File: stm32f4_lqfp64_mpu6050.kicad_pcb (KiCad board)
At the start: 2 copper layers, 35.5 x 35.2 mm, 74 parts, among them M1 ALIS-CUSTOM-PARTS_POWERPADS, M2 ALIS-CUSTOM-PARTS_POWERPADS, M3 ALIS-CUSTOM-PARTS_POWERPADS, M4 ALIS-CUSTOM-PARTS_POWERPADS, M5 ALIS-CUSTOM-PARTS_POWERPADS, Q1 CRYSTAL_50X32, Q2 BSS138, Q3 BSS138, Q4 BSS138, Q5 BSS138, Q6 BSS138, U1 STM32_STM32F10XRXT6, U2 MPU6050, U3 LP2985LV, U4 ublox_neo7, X1 CON-JST_SM04B-SRSS-TB, X2 CON-JST_SM04B-SRSS-TB, X3 CON-JST_SM04B-SRSS-TB, X4 CON-JST_SM04B-SRSS-TB, X5 CON-JST_SM04B-SRSS-TB, X6 CON-JST_SM04B-SRSS-TB, X7 CON-JST_SM04B-SRSS-TB, X8 CON-JST_SM04B-SRSS-TB

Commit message: added lots of stuff
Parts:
- added C24: 100n, Capacitors_SMD:C_0402, F.Cu at (158.5, 107.1)
- added C25: 220n, Capacitors_SMD:C_0402, F.Cu at (156.5, 113.5)
- added C26: 4u7, Capacitors_SMD:C_0805, F.Cu at (159.0, 113.5)
- added C27: 100n, Capacitors_SMD:C_0402, F.Cu at (151.8, 95.0)
- added C28: 100n, Capacitors_SMD:C_0402, F.Cu at (157.0, 93.7)
- added C29: 4.7u, Capacitors_SMD:C_0603, F.Cu at (155.7, 110.5)
- added C30: CP, alis_parts:DSK-3R3H204T614-H2L, B.Cu at (140.8, 100.1)
- added C31: 2.2uF Tantalum, Capacitors_SMD:C_0603, F.Cu at (164.0, 112.0)
- added C32: 470p, Capacitors_SMD:C_0402, F.Cu at (161.7, 111.8)
- added C33: 1uF, Capacitors_SMD:C_0402, F.Cu at (161.7, 106.2)
- added D10: D_Schottky, Diodes_SMD:SOD-323, B.Cu at (145.9, 105.0)
- added R5: 2k2, Resistors_SMD:R_0402, F.Cu at (151.0, 102.0)
- added R6: 2k2, Resistors_SMD:R_0402, F.Cu at (151.0, 103.1)
- added R7: 100R, Resistors_SMD:R_0402, B.Cu at (145.9, 103.4)
- added R8: 2k, Resistors_SMD:R_0402, F.Cu at (138.0, 114.7)
- added U5: HMC5883L, alis_parts:LCC16, F.Cu at (158.5, 110.0)
- added U6: BMP180, alis_parts:LGA7, F.Cu at (155.2, 96.4)
- added U7: MIC5205, TO_SOT_Packages_SMD:SOT-23-5, F.Cu at (162.7, 108.7)
- R4: value 0R -> 10k
- U1: value STM32_STM32F10XRXT6 -> STM32F405R
- moved M5 36.4 mm to (132.5, 92.5), turned to 270 degrees
- moved Q6 30.2 mm to (134.9, 95.0), turned to 90 degrees
- moved C13 4.28 mm to (152.1, 109.7), turned to 180 degrees
- moved C16 4.24 mm to (156.8, 107.1), turned to 90 degrees
- moved U2 3.42 mm to (153.5, 106.4)
- moved C15 2.94 mm to (154.3, 110.7)
- moved C14 2.72 mm to (154.6, 102.4)
- moved R1 2.56 mm to (150.4, 106.0), turned to 90 degrees
- moved R18 0.76 mm to (156.2, 100.3)
- moved C8 0.63 mm to (149.9, 108.5)
- moved R17 0.63 mm to (156.2, 99.1)
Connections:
- C16 pad 1: VCC -> VCC_SEN
- U1 pad 14: Net-(U1-Pad14) -> LED_RED
- U1 pad 15: Net-(U1-Pad15) -> LED_BLUE
- U1 pad 2: LED_RED -> MCU_BUZZER
- U1 pad 3: LED_BLUE -> Net-(U1-Pad3)
- U1 pad 42: MCU_BUZZER -> Net-(U1-Pad42)
- U2 pad 13: VCC -> VCC_SEN
- U4 pad 22: Net-(U4-Pad22) -> V_BCKP
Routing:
- net VCC_SEN: track 0.00 -> 40.6 mm, vias 0 -> 3
- net GND: track 141.9 -> 182.2 mm, vias 15 -> 27
- net SDA: track 8.09 -> 33.0 mm, vias 0 -> 3
- net VCC: track 143.3 -> 163.2 mm, vias 12 -> 13
- net TX3: track 2.20 -> 20.6 mm
- net SCL: track 8.90 -> 24.3 mm, vias 0 -> 2
- net MCU_BUZZER: track 16.8 -> 5.11 mm
- net V_BCKP: track 0.00 -> 10.6 mm
- net VCCEXT: track 156.3 -> 146.2 mm
- net Net-(C25-Pad1): track 0.00 -> 8.60 mm
- net TX4: track 22.3 -> 18.0 mm
- net +5V_USB: track 16.9 -> 19.9 mm
- net LED_RED: track 14.4 -> 11.3 mm
- net LED_BLUE: track 19.5 -> 16.7 mm
- net Net-(C25-Pad2): track 0.00 -> 2.54 mm
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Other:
- rule pad_to_mask_clearance: 0.2 -> 0.1
- board text added: "F4 Autopilot v0.1 © Alexander Tuxen 2016"
- board text removed: "Minimal F4 FC v0.1 (c) Alexander Tuxen 2016"

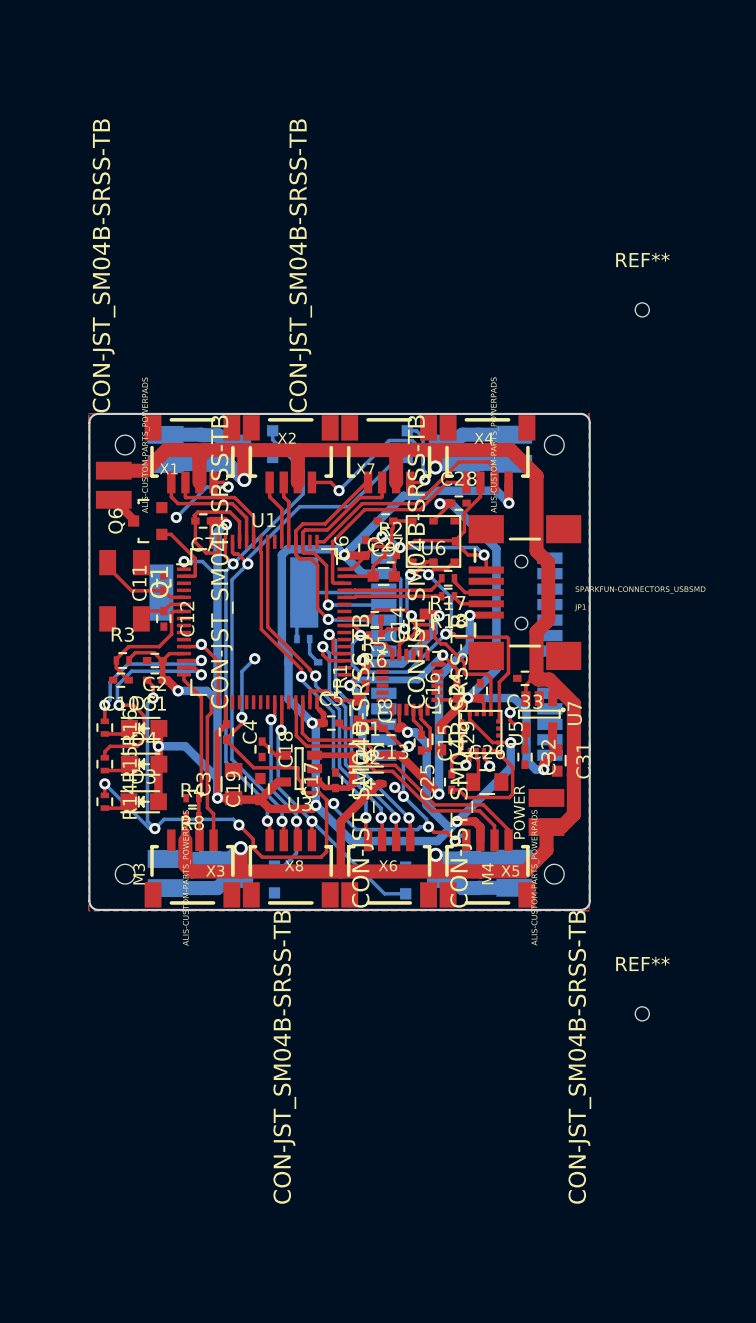
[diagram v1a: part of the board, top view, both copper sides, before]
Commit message: began to add support for video overlay
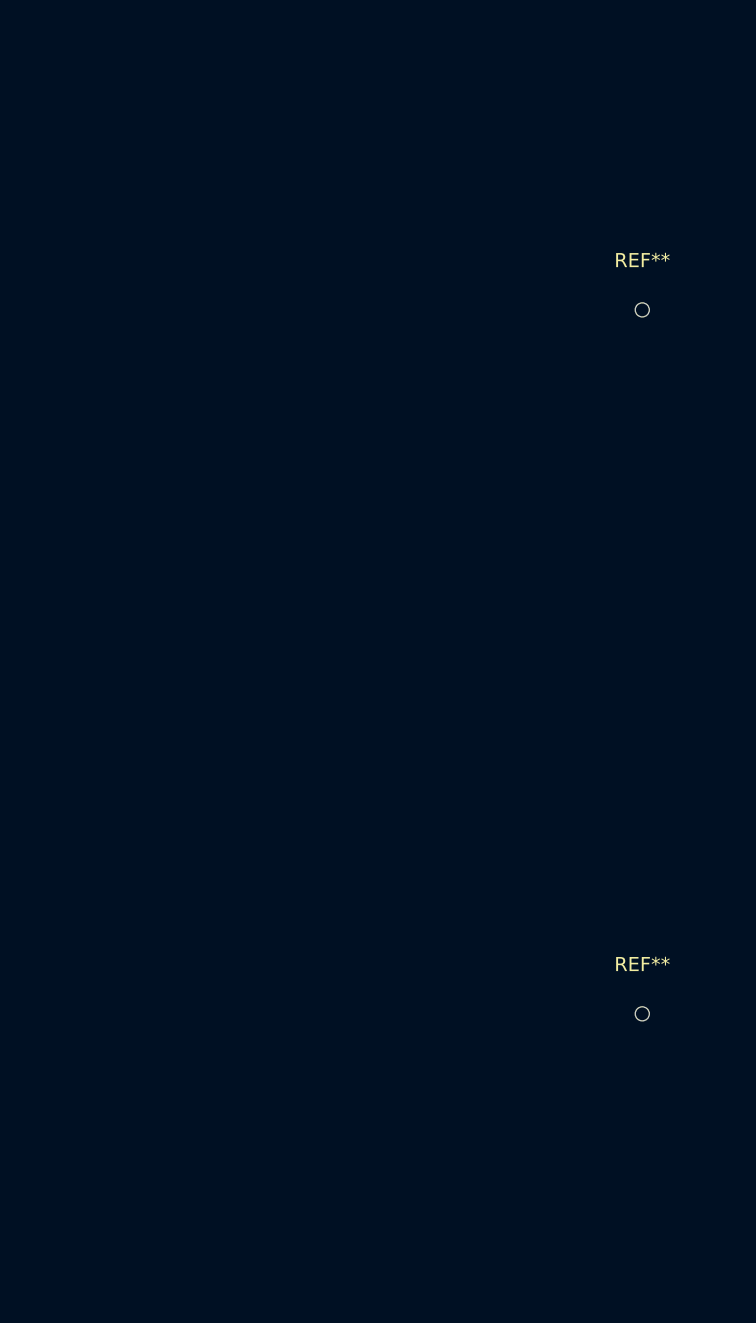
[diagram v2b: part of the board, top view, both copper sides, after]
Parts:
- removed @HOLE0, @HOLE1, @HOLE2, @HOLE3: , 
- removed C1, C17: 1u, Capacitors_SMD:C_0402
- removed C10, C15, C16, C2, C20, C21, C22, C23, C24, C27, C28, C4, C5, C6, C7: 100n, Capacitors_SMD:C_0402
- removed C11, C12: 22p, Capacitors_SMD:C_0402
- removed C13, C18: 10n, Capacitors_SMD:C_0402
- removed C14: 2.2n/50V, Capacitors_SMD:C_0603
- removed C19, C8, C9: 2.2u, Capacitors_SMD:C_0603
- removed C25: 220n, Capacitors_SMD:C_0402
- removed C26: 4u7, Capacitors_SMD:C_0805
- removed C29: 4.7u, Capacitors_SMD:C_0603
- removed C3: 4.7u, Capacitors_SMD:C_0805
- removed C30: CP, alis_parts:DSK-3R3H204T614-H2L
- removed C31: 2.2uF Tantalum, Capacitors_SMD:C_0603
- removed C32: 470p, Capacitors_SMD:C_0402
- removed C33: 1uF, Capacitors_SMD:C_0402
- removed D1, D2: D_Schottky_Small, Diodes_SMD:SOD-323
- removed D10: D_Schottky, Diodes_SMD:SOD-323
- removed D3: Green, LEDs:LED-0805
- removed D4: Blue, LEDs:LED-0805
- removed D5: Red, LEDs:LED-0805
- removed D6, D7, D8, D9: D, Diodes_SMD:SOD-323
- removed JP1: SPARKFUN-CONNECTORS_USBSMD, USB-MINIB
- removed M1, M2, M3, M4, M5: ALIS-CUSTOM-PARTS_POWERPADS, minimal:ALIS-CUSTOM-PARTS_PAD-JUMPER-2-NO_YES_SILK
- removed POWER: , PAD-JUMPER-2-NO_YES_SILK
- removed Q1: CRYSTAL_50X32, minimal:CRYSTAL_50X32
- removed Q2, Q3, Q4, Q5, Q6: BSS138, TO_SOT_Packages_SMD:SOT-23
- removed R1, R2: 0R, Resistors_SMD:R_0402
- removed R14, R15, R16, R7: 100R, Resistors_SMD:R_0402
- removed R17, R18: 22R, Resistors_SMD:R_0402
- removed R3, R4: 10k, Resistors_SMD:R_0402
- removed R5, R6: 2k2, Resistors_SMD:R_0402
- removed R8: 2k, Resistors_SMD:R_0402
- removed U1: STM32F405R, Housings_QFP:LQFP-64_10x10mm_Pitch0.5mm
- removed U2: MPU6050, QFN-24-noEP_4x4mm_Pitch0.5mm
- removed U3: LP2985LV, TO_SOT_Packages_SMD:SOT-23-5
- removed U4: ublox_neo7, alis_parts:ublox_neo7
- removed U5: HMC5883L, alis_parts:LCC16
- removed U6: BMP180, alis_parts:LGA7
- removed U7: MIC5205, TO_SOT_Packages_SMD:SOT-23-5
- removed X1, X2, X3, X4, X5, X6, X7, X8: CON-JST_SM04B-SRSS-TB, SM04B-SRSS-TB
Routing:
- net GND: track 182.2 -> 0.00 mm, vias 27 -> 0
- net VCC: track 163.2 -> 0.00 mm, vias 13 -> 0
- net VCCEXT: track 146.2 -> 0.00 mm, vias 4 -> 0
- net VCC_SEN: track 40.6 -> 0.00 mm, vias 3 -> 0
- net PWM7: track 38.5 -> 0.00 mm, vias 2 -> 0
- net PWM8: track 35.4 -> 0.00 mm, vias 2 -> 0
- net SDA: track 33.0 -> 0.00 mm, vias 3 -> 0
- net PWM1: track 24.6 -> 0.00 mm, vias 2 -> 0
- net PWM2: track 24.4 -> 0.00 mm, vias 2 -> 0
- net SCL: track 24.3 -> 0.00 mm, vias 2 -> 0
- net RX3: track 20.9 -> 0.00 mm
- net TX3: track 20.6 -> 0.00 mm
- net +5V_USB: track 19.9 -> 0.00 mm, vias 2 -> 0
- net PWM4: track 19.7 -> 0.00 mm, vias 2 -> 0
- net PWM6: track 19.2 -> 0.00 mm, vias 2 -> 0
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- removed copper zone on B.Cu, net GND
- removed copper zone on F.Cu, net GND
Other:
- board outline removed
- board text removed: "+ -"
- board text removed: "F4 Autopilot v0.1 © Alexander Tuxen 2016"

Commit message: OSD running on breadboard
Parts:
- removed the REF** at (120.0, 80.0)
- removed the REF** at (170.0, 80.0)
- removed the REF** at (170.0, 130.0)
- removed the REF** at (120.0, 130.0)
- added C1: 100n, Capacitors_SMD:C_0402, F.Cu at (339.5, 71.9)
- added C10: 1u, Capacitors_SMD:C_0402, F.Cu at (255.6, 100.7)
- added C11: 100n, Capacitors_SMD:C_0402, F.Cu at (260.9, 106.6)
- added C12: 100n, Capacitors_SMD:C_0402, F.Cu at (245.2, 119.5)
- added C13: 22p, Capacitors_SMD:C_0402, F.Cu at (259.5, 100.7)
- added C14: 22p, Capacitors_SMD:C_0402, F.Cu at (249.5, 118.7)
- added C15: 2.2u, Capacitors_SMD:C_0603, F.Cu at (247.4, 100.9)
- added C16: 2.2u, Capacitors_SMD:C_0603, F.Cu at (251.6, 100.9)
- added C17: 10n, Capacitors_SMD:C_0402, F.Cu at (327.3, 108.8)
- added C18: 100n, Capacitors_SMD:C_0402, F.Cu at (323.0, 108.8)
- added C19: 4.7u, Capacitors_SMD:C_0603, F.Cu at (330.8, 102.7)
- added C2: 100n, Capacitors_SMD:C_0402, F.Cu at (344.8, 65.8)
- added C20: 2.2n/50V, Capacitors_SMD:C_0603, F.Cu at (324.7, 102.7)
- added C21: 100n, Capacitors_SMD:C_0402, F.Cu at (331.6, 108.8)
- added C22: 1u, Capacitors_SMD:C_0402, F.Cu at (340.7, 93.6)
- added C23: 2.2u, Capacitors_SMD:C_0603, F.Cu at (341.3, 81.7)
- added C24: 1u, Capacitors_SMD:C_0402, F.Cu at (336.9, 93.6)
- added C25: 2.2u, Capacitors_SMD:C_0603, F.Cu at (337.1, 81.7)
- added C26: 10n, Capacitors_SMD:C_0402, F.Cu at (340.7, 87.7)
- added C27: 10n, Capacitors_SMD:C_0402, F.Cu at (336.9, 87.7)
- added C28: 100n, Capacitors_SMD:C_0402, F.Cu at (204.0, 140.1)
- added C29: C, Capacitors_SMD:C_0402, F.Cu at (212.0, 134.2)
- added C3: 100n, Capacitors_SMD:C_0402, F.Cu at (349.5, 65.6)
- added C30: 100n, Capacitors_SMD:C_0402, F.Cu at (207.7, 134.2)
- added C31: 100n, Capacitors_SMD:C_0402, F.Cu at (212.5, 128.4)
- added C32: 100n, Capacitors_SMD:C_0402, F.Cu at (207.7, 128.4)
- added C4: 100n, Capacitors_SMD:C_0402, F.Cu at (344.8, 71.7)
- added C5: 4.7u, Capacitors_SMD:C_0805, F.Cu at (243.0, 101.1)
- added C6: 100n, Capacitors_SMD:C_0402, F.Cu at (256.2, 112.4)
- added C7: 100n, Capacitors_SMD:C_0402, F.Cu at (251.5, 112.8)
- added C8: 100n, Capacitors_SMD:C_0402, F.Cu at (256.2, 106.6)
- added C9: 100n, Capacitors_SMD:C_0402, F.Cu at (251.5, 107.0)
- added D1: Green, LEDs:LED-0805, F.Cu at (349.0, 59.7)
- added D2: Blue, LEDs:LED-0805, F.Cu at (340.1, 66.0)
- added D3: Red, LEDs:LED-0805, F.Cu at (334.8, 67.6)
- added D4: D, Diodes_SMD:SOD-323, F.Cu at (330.6, 67.7)
- added D5: D, Diodes_SMD:SOD-323, F.Cu at (343.6, 53.7)
- added D6: D, Diodes_SMD:SOD-323, F.Cu at (339.7, 53.7)
- added D7: D, Diodes_SMD:SOD-323, F.Cu at (339.7, 59.9)
- added D8: D_Schottky_Small, Diodes_SMD:SOD-323, F.Cu at (319.6, 87.8)
- added D9: D_Schottky_Small, Diodes_SMD:SOD-323, F.Cu at (319.6, 81.6)
- added JP1: SPARKFUN-CONNECTORS_USBSMD, minimal:SPARKFUN-CONNECTORS_USB-MINIB, F.Cu at (104.9, 119.7)
- added M1: ALIS-CUSTOM-PARTS_POWERPADS, minimal:ALIS-CUSTOM-PARTS_PAD-JUMPER-2-NO_YES_SILK, F.Cu at (313.9, 58.6)
- added M2: ALIS-CUSTOM-PARTS_POWERPADS, minimal:ALIS-CUSTOM-PARTS_PAD-JUMPER-2-NO_YES_SILK, F.Cu at (313.9, 53.6)
- added M3: ALIS-CUSTOM-PARTS_POWERPADS, minimal:ALIS-CUSTOM-PARTS_PAD-JUMPER-2-NO_YES_SILK, F.Cu at (325.1, 53.6)
- added M4: ALIS-CUSTOM-PARTS_POWERPADS, minimal:ALIS-CUSTOM-PARTS_PAD-JUMPER-2-NO_YES_SILK, F.Cu at (313.9, 63.7)
- added M5: ALIS-CUSTOM-PARTS_POWERPADS, minimal:ALIS-CUSTOM-PARTS_PAD-JUMPER-2-NO_YES_SILK, F.Cu at (325.1, 58.6)
- added P1: CONN_01X03, Pin_Headers:Pin_Header_Angled_1x03, B.Cu at (165.4, 97.5)
- added P2: CONN_01X03, Pin_Headers:Pin_Header_Angled_1x03, B.Cu at (168.7, 97.5)
- added P3: CONN_01X03, Pin_Headers:Pin_Header_Angled_1x03, B.Cu at (168.5, 107.0)
- added P4: CONN_01X03, Pin_Headers:Pin_Header_Angled_1x03, B.Cu at (165.4, 107.0)
- added Q1: BSS138, TO_SOT_Packages_SMD:SOT-23, F.Cu at (318.6, 69.2)
- added Q2: BSS138, TO_SOT_Packages_SMD:SOT-23, F.Cu at (334.4, 61.1)
- added Q3: BSS138, TO_SOT_Packages_SMD:SOT-23, F.Cu at (325.3, 64.2)
- added Q4: BSS138, TO_SOT_Packages_SMD:SOT-23, F.Cu at (334.4, 54.1)
- added Q5: BSS138, TO_SOT_Packages_SMD:SOT-23, F.Cu at (311.9, 69.2)
- added Q6: CRYSTAL_50X32, minimal:CRYSTAL_50X32, F.Cu at (233.7, 116.9)
- added R1: 10k, Resistors_SMD:R_0402, F.Cu at (257.8, 88.5)
- added R10: 10k, Resistors_SMD:R_0402, F.Cu at (247.2, 107.1)
- added R11: 0R, Resistors_SMD:R_0402, F.Cu at (244.8, 113.5)
- added R12: 0R, Resistors_SMD:R_0402, F.Cu at (242.7, 107.5)
- added R13: 680k, Resistors_SMD:R_0402, F.Cu at (199.3, 137.9)
- added R14: 470, Resistors_SMD:R_0402, F.Cu at (190.7, 138.2)
- added R15: 470, Resistors_SMD:R_0402, F.Cu at (194.5, 138.2)
- added R2: 22R, Resistors_SMD:R_0402, F.Cu at (296.7, 53.7)
- added R3: 2k, Resistors_SMD:R_0402, F.Cu at (293.3, 53.7)
- added R4: 22R, Resistors_SMD:R_0402, F.Cu at (261.6, 88.5)
- added R5: 15k, Resistors_SMD:R_0402, F.Cu at (250.5, 88.5)
- added R6: 15k, Resistors_SMD:R_0402, F.Cu at (254.2, 91.4)
- added R7: 100R, Resistors_SMD:R_0402, F.Cu at (324.3, 70.8)
- added R8: 100R, Resistors_SMD:R_0402, F.Cu at (344.1, 59.9)
- added R9: 100R, Resistors_SMD:R_0402, F.Cu at (347.9, 53.7)
- added REF**: alibenpeng!, rcexplorer_tricopter, F.Cu at (145.3, 104.6)
- added REF**: PositioningHole_1mm, alis_parts:PositioningHole_1mm, F.Cu at (83.1, 155.0)
- added REF**: PositioningHole_1mm, alis_parts:PositioningHole_1mm, F.Cu at (83.1, 55.0)
- added REF**: PositioningHole_1mm, alis_parts:PositioningHole_1mm, F.Cu at (213.1, 55.0)
- added REF**: PositioningHole_1mm, alis_parts:PositioningHole_1mm, F.Cu at (213.1, 155.0)
- added U1: STM32F405R, Housings_QFP:LQFP-64_10x10mm_Pitch0.5mm, F.Cu at (115.2, 104.5)
- added U2: MPU6050, Housings_DFN_QFN:QFN-24-1EP_4x4mm_Pitch0.5mm, F.Cu at (135.9, 104.1)
- added U3: LP2985LV, TO_SOT_Packages_SMD:SOT-23-5, F.Cu at (330.9, 89.7)
- added U4: LP2985LV, TO_SOT_Packages_SMD:SOT-23-5, F.Cu at (330.9, 82.3)
- added U5: TS5A3160, TO_SOT_Packages_SMD:SC-70-6, F.Cu at (192.9, 129.7)
- added U6: LM1881, Housings_SOIC:SOIC-8_3.9x4.9mm_Pitch1.27mm, F.Cu at (174.0, 118.0)
- added U7: TS5A3160, TO_SOT_Packages_SMD:SC-70-6, F.Cu at (184.6, 129.7)
- added U8: TS5A3160, TO_SOT_Packages_SMD:SC-70-6, F.Cu at (184.6, 139.4)
- added X1: CON-JST_SM04B-SRSS-TB, Connectors_JST_SH:Connectors_JST_SM04B-SRSS-TB, F.Cu at (281.1, 55.8)
- added X2: CON-JST_SM04B-SRSS-TB, Connectors_JST_SH:Connectors_JST_SM04B-SRSS-TB, F.Cu at (103.1, 89.0)
- added X3: CON-JST_SM04B-SRSS-TB, Connectors_JST_SH:Connectors_JST_SM04B-SRSS-TB, F.Cu at (256.1, 57.3)
- added X4: CON-JST_SM04B-SRSS-TB, Connectors_JST_SH:Connectors_JST_SM04B-SRSS-TB, F.Cu at (116.3, 120.8)
- added X5: CON-JST_SM04B-SRSS-TB, Connectors_JST_SH:Connectors_JST_SM04B-SRSS-TB, F.Cu at (259.5, 55.8)
- added X6: CON-JST_SM04B-SRSS-TB, Connectors_JST_SH:Connectors_JST_SM04B-SRSS-TB, F.Cu at (190.0, 93.2)
- added X7: CON-JST_SM04B-SRSS-TB, Connectors_JST_SH:Connectors_JST_SM04B-SRSS-TB, B.Cu at (166.8, 118.2)
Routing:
- added copper zone on B.Cu, net GND
- added copper zone on F.Cu, net GND
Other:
- board outline added: 130 x 100 mm
- copper layers 2 -> 4
- net class Default: clearance 0.1778 -> 0.4; via_dia 0.8 -> 0.6
- net class Power removed
- rule pad_to_mask_clearance: 0.1 -> 0.0508
- rule trace_clearance: 0.1778 -> 0.4
- rule trace_min: 0.1 -> 0.2
- board text added: "alibenpeng!"

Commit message: power traces routed
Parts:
- removed D4, D5, D6, D7: D, Diodes_SMD:SOD-323
- removed M1, M2, M3, M4: ALIS-CUSTOM-PARTS_POWERPADS, minimal:ALIS-CUSTOM-PARTS_PAD-JUMPER-2-NO_YES_SILK
- removed P3, P4: CONN_01X03, Pin_Headers:Pin_Header_Angled_1x03
- removed Q1, Q2, Q3, Q4: BSS138, TO_SOT_Packages_SMD:SOT-23
- removed X5, X6, X7: CON-JST_SM04B-SRSS-TB, Connectors_JST_SH:Connectors_JST_SM04B-SRSS-TB
- added C33: 4u7, Capacitors_Tantalum_SMD:TantalC_SizeA_EIA-3216_Reflow, F.Cu at (168.4, 93.0)
- added JP2: Jumper_NO_Small, minimal:ALIS-CUSTOM-PARTS_PAD-JUMPER-2-NO_YES_SILK, F.Cu at (125.6, 107.2)
- added REF**: PositioningHole_1mm, alis_parts:PositioningHole_1mm, F.Cu at (144.1, 105.0)
- added W1: TEST_1P, Measurement_Points:Measurement_Point_Square-SMD-Pad_Big, F.Cu at (165.1, 85.1)
- added W2: TEST_1P, Measurement_Points:Measurement_Point_Square-SMD-Pad_Big, F.Cu at (167.6, 85.1)
- added W3: TEST_1P, Measurement_Points:Measurement_Point_Square-SMD-Pad_Big, F.Cu at (170.2, 85.1)
- added W4: TEST_1P, Measurement_Points:Measurement_Point_Square-SMD-Pad_Big, F.Cu at (172.7, 85.1)
- C1, C10, C11, C12, C13, C14, C17, C18, C2, C21, C22, C24, C26, C27, C28, C29, C30, C31, C32, C6, C7, C8, C9: footprint Capacitors_SMD:C_0402 -> Capacitors_SMD:C_0603
- C3: value 100n -> 2.2u; footprint Capacitors_SMD:C_0402 -> Capacitors_SMD:C_0603
- C4: value 100n -> 4u7; footprint Capacitors_SMD:C_0402 -> Capacitors_Tantalum_SMD:TantalC_SizeA_EIA-3216_Reflow
- P1: value CONN_01X03 -> CONN_01X08; footprint Pin_Headers:Pin_Header_Angled_1x03 -> Pin_Headers:Pin_Header_Straight_1x08
- P2: value CONN_01X03 -> CONN_02X08; footprint Pin_Headers:Pin_Header_Angled_1x03 -> Pin_Headers:Pin_Header_Straight_2x08
- R1, R10, R13, R14, R15, R2, R4, R5, R6, R7, R8, R9: footprint Resistors_SMD:R_0402 -> Resistors_SMD:R_0603
- R11, R12: value 0R -> 10k; footprint Resistors_SMD:R_0402 -> Resistors_SMD:R_0603
- R3: value 2k -> 10k; footprint Resistors_SMD:R_0402 -> Resistors_SMD:R_0603
- U5: value TS5A3160 -> W25Q80BV; footprint TO_SOT_Packages_SMD:SC-70-6 -> Housings_SOIC:SOIJ-8_5.3x5.3mm_Pitch1.27mm
- U7, U8: footprint TO_SOT_Packages_SMD:SC-70-6 -> TO_SOT_Packages_SMD:SOT-23-6
- moved R9 245.0 mm to (111.8, 119.1), turned to 270 degrees
- moved D1 241.5 mm to (115.8, 122.4), turned to 270 degrees
- moved C22 240.1 mm to (100.8, 102.7), turned to 270 degrees
- moved C23 238.2 mm to (103.9, 101.1), turned to 180 degrees
- moved R8 237.8 mm to (113.8, 119.1), turned to 270 degrees
- moved C26 237.3 mm to (104.1, 105.9), turned to 180 degrees
- moved C3 233.4 mm to (121.7, 116.2)
- moved D2 233.3 mm to (113.8, 122.4), turned to 270 degrees
- moved D3 229.7 mm to (111.8, 122.4), turned to 270 degrees
- moved U3 227.8 mm to (103.5, 103.5)
- moved D8 219.0 mm to (101.6, 108.3), turned to 270 degrees
- moved D9 217.6 mm to (103.6, 108.3), turned to 270 degrees
- moved R7 214.0 mm to (115.8, 119.1), turned to 270 degrees
- moved C27 206.1 mm to (131.2, 101.0)
- moved C24 203.4 mm to (133.5, 96.0), turned to 180 degrees
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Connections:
- C1 pad 1: M4 -> GND
- C1 pad 2: VBAT -> 3.3V
- C2 pad 1: M3 -> GND
- C2 pad 2: VBAT -> 3.3V
- C29 pad 2: Net-(C29-Pad2) -> VIDEO_IN
- C3 pad 1: M1 -> GND
- C3 pad 2: VBAT -> 3.3V
- C4 pad 1: M2 -> VBAT
- C4 pad 2: VBAT -> GND
- P1 pad 1: TIM5_CH1 -> VIDEO_IN
- P1 pad 2: VBAT -> TIM8_CH3
- P1 pad 3: GND -> TIM12_CH2
- P2 pad 1: TIM5_CH2 -> VIDEO_OUT
- P2 pad 2: VBAT -> GND
- P2 pad 3: GND -> TIM5_CH4
- R1 pad 1: VBAT -> MCU_BUZZER
- R1 pad 2: TX2/ADC123_IN2 -> GND
- R11 pad 1: Net-(C15-Pad1) -> BW_MASK
- R12 pad 1: Net-(C16-Pad1) -> Net-(JP2-Pad2)
- R3 pad 1: TX2/ADC123_IN2 -> BW_LEVEL
- U1 pad 35: TIM12_CH1 -> TIM12_CH1/PPM
- U1 pad 60: GND -> Net-(JP2-Pad2)
- U5 pad 1: VIDEO_IN2 -> FLASH_CS
- U5 pad 2: GND -> MISO
- U5 pad 3: VIDEO_IN1 -> 3.3V
- U5 pad 4: Net-(C29-Pad2) -> GND
- U5 pad 5: 3.3V -> MOSI
- U5 pad 6: VIDEO1_2 -> SCK
- U7 pad 3: Net-(C29-Pad2) -> VIDEO_IN
- X3 pad 4: TIM8_CH1 -> TIM12_CH1
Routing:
- net 3.3V: track 0.00 -> 189.1 mm, vias 0 -> 6
- net VBAT: track 0.00 -> 158.5 mm, vias 0 -> 6
- net reg_vin: track 0.00 -> 70.4 mm, vias 0 -> 2
- net USBD_N: track 0.00 -> 12.5 mm
- net GND: track 0.00 -> 12.3 mm
- net USBD_P: track 0.00 -> 10.3 mm
- net Net-(C13-Pad1): track 0.00 -> 10.1 mm
- net +5V_USB: track 0.00 -> 8.92 mm
- net 3.3V_SEN: track 0.00 -> 8.89 mm
- net /RESET: track 0.00 -> 7.42 mm
- net Net-(C14-Pad1): track 0.00 -> 6.15 mm
- net D+: track 0.00 -> 4.70 mm
- net reg_bypass: track 0.00 -> 3.64 mm
- net D-: track 0.00 -> 3.37 mm
- net BUZZER: track 0.00 -> 2.73 mm
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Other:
- net class Default: clearance 0.4 -> 0.25; via_dia 0.6 -> 0.8
- net class VCC added: clearance 0.25, trace_width 0.4, via_dia 0.8, via_drill 0.4
- net class power added: clearance 0.25, trace_width 1, via_dia 0.8, via_drill 0.4
- rule trace_clearance: 0.4 -> 0.25
- board text added: "Y Center: 104.97"

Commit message: routing done except for ground, but ugly
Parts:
- moved C3 2.45 mm to (119.4, 117.1)
- moved U5 2.34 mm to (125.7, 114.8)
- moved X3 1.53 mm to (118.9, 88.4)
- moved X1 0.90 mm to (111.0, 88.4)
- moved X4 0.76 mm to (120.8, 121.7)
- moved X2 0.64 mm to (103.1, 88.4)
- turned R5 to 0 degrees
- turned R6 to 0 degrees
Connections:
- C26 pad 1: reg_bypass -> Net-(C26-Pad1)
- C27 pad 1: reg_bypass -> Net-(C27-Pad1)
- U3 pad 4: reg_bypass -> Net-(C26-Pad1)
- U4 pad 4: reg_bypass -> Net-(C27-Pad1)
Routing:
- net TIM8_CH2/FRSKY_RSSI/DSM: track 0.00 -> 101.9 mm, vias 0 -> 2
- net ADC3: track 0.00 -> 77.1 mm, vias 0 -> 2
- net TIM5_CH4: track 0.00 -> 71.6 mm, vias 0 -> 2
- net TIM8_CH1: track 0.00 -> 68.6 mm, vias 0 -> 1
- net BW_MASK: track 0.00 -> 67.8 mm, vias 0 -> 2
- net TIM12_CH1/PPM: track 0.00 -> 66.3 mm, vias 0 -> 1
- net TIM12_CH2: track 0.00 -> 66.0 mm, vias 0 -> 1
- net BW_LEVEL: track 0.00 -> 65.7 mm, vias 0 -> 2
- net TIM5_CH2: track 0.00 -> 65.4 mm, vias 0 -> 1
- net TIM5_CH3: track 0.00 -> 65.3 mm, vias 0 -> 1
- net TIM8_CH3: track 0.00 -> 65.1 mm, vias 0 -> 1
- net VSYNC_EXTI: track 0.00 -> 63.7 mm, vias 0 -> 2
- net TIM8_CH4: track 0.00 -> 62.4 mm, vias 0 -> 3
- net TIM5_CH1: track 0.00 -> 62.2 mm, vias 0 -> 1
- net ADC1: track 0.00 -> 60.4 mm, vias 0 -> 2
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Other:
- net class Default: clearance 0.25 -> 0.2; trace_width 0.25 -> 0.2
- rule trace_clearance: 0.25 -> 0.2
